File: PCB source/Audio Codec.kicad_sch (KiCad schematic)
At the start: 25 parts, among them J3 JST XH, U8 TDA7052A, U9 PCM2704CDBR, X1 X322512MSB4SI

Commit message: Figure out SSPND pin
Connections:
- net VDD_{int}: no longer U9.27 (~{SSPND})
- net VCCL: now reaches C35.1, U9.13 (VCCL)
- net VCCR: now reaches C38.1, U9.16 (VCCR)
- net VCCP: now reaches C39.1, U9.20 (VCCP)
- no-connect marks 5 -> 6
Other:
- moved on the sheet: C32, C33, C34, C35, C38, C39

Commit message: Prepare board for layout
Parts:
- removed R19: 1.5kΩ, PCM_JLCPCB:R_0402, symbol PCM_JLCPCB-Resistors:0402,1.5kΩ
- removed R20, R21: 22Ω, PCM_JLCPCB:R_0402, symbol PCM_JLCPCB-Resistors:0402,22Ω
- added R42: 1.5kΩ, PCM_JLCPCB:R_0603, symbol PCM_JLCPCB-Resistors:0603,1.5kΩ
- RV1: value 1Meg Bourns 3296 -> RM065 1Meg; footprint Potentiometer_THT:Potentiometer_Bourns_3296W_Vertical -> Potentiometer_THT:Potentiometer_Runtron_RM-065_Vertical
- U8: footprint (none) -> Package_SO:SO-8_3.9x4.9mm_P1.27mm
- U9: footprint PCM2704CDBR:SOP65P780X200-28N -> PCM2704:SOP65P780X200-28N
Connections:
- net VDD_{int}: now also R42.1
- net D+ renamed USB_AUDIO.D+
- net USB_AUDIO.D+: now also R42.2
- net D- renamed USB_AUDIO.D-

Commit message: Do buck Layout
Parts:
- removed R42: 1.5kΩ, PCM_JLCPCB:R_0603, symbol PCM_JLCPCB-Resistors:0603,1.5kΩ
- added R19: 1.5kΩ, PCM_JLCPCB:R_0402, symbol PCM_JLCPCB-Resistors:0402,1.5kΩ
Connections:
- net USB_AUDIO.D+: now also R19.2
- net VDD_{int}: now also R19.1
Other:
- moved on the sheet: C40

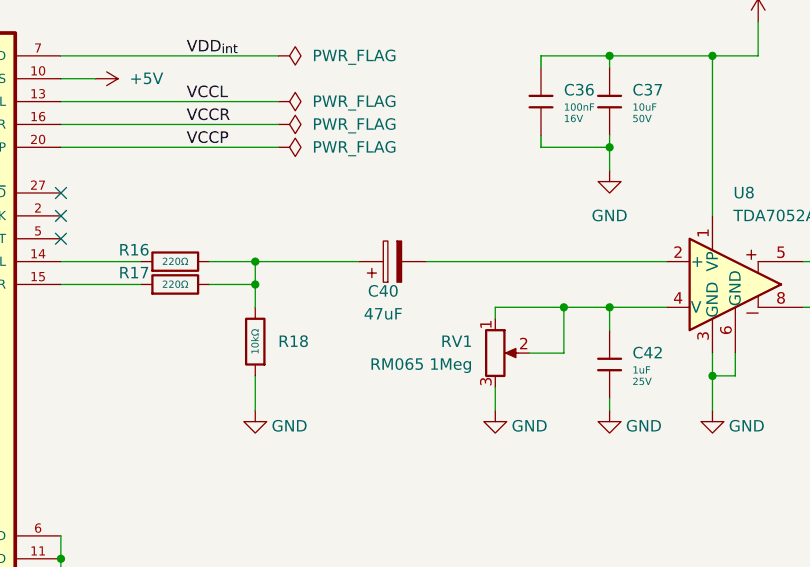
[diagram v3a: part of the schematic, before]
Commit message: Create v1 floorplan
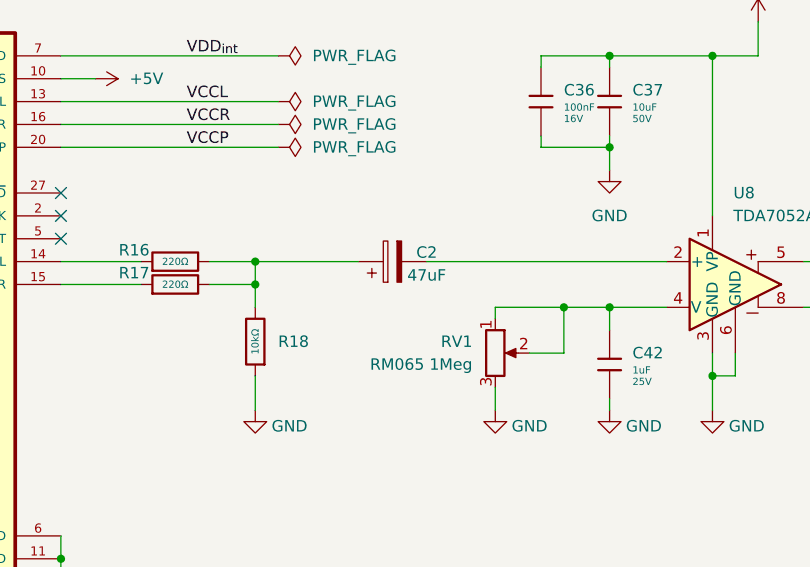
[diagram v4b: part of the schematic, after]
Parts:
- removed C40: 47uF, Capacitor_SMD:CP_Elec_6.3x5.4, symbol Device:C_Polarized
- added C2: 47uF, Capacitor_SMD:CP_Elec_4x5.4, symbol Device:C_Polarized
- C41: footprint Capacitor_SMD:CP_Elec_6.3x5.4 -> Capacitor_SMD:CP_Elec_4x5.4
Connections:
- net at R16.2, R17.2, R18.2: now also C2.1
- net at U8.2 (+): now also C2.2
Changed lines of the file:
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@@
 	)
 	(symbol
-		(lib_id "Device:C_Polarized")
-		(at 177.8 86.36 90)
-		(unit 1)
-		(exclude_from_sim no)
-		(in_bom yes)
-		(on_board yes)
-		(dnp no)
-		(property "Reference" "C40"
-			(at 176.784 89.662 90)
-			(effects
-				(font
-					(size 1.27 1.27)
-				)
-			)
-		)
-		(property "Value" "47uF"
-			(at 176.784 92.202 90)
-			(effects
-				(font
-					(size 1.27 1.27)
-				)
-			)
-		)
-		(property "Footprint" "Capacitor_SMD:CP_Elec_6.3x5.4"
-			(at 181.61 85.3948 0)
-			(effects
-				(font
-					(size 1.27 1.27)
-				)
-				(hide yes)
-			)
-		)
-		(property "Datasheet" "~"
-			(at 177.8 86.36 0)
-			(effects
-				(font
-					(size 1.27 1.27)
-				)
-				(hide yes)
-			)
-		)
-		(property "Description" "Polarized capacitor"
-			(at 177.8 86.36 0)
-			(effects
-				(font
-					(size 1.27 1.27)
-				)
-				(hide yes)
-			)
-		)
-		(property "LCSC" " C90276"
-			(at 177.8 86.36 90)
-			(effects
-				(font
-					(size 1.27 1.27)
-				)
-				(hide yes)
-			)
-		)
-		(property "MPN" "VT1V470M0605"
-			(at 177.8 86.36 90)
-			(effects
-				(font
-					(size 1.27 1.27)
-				)
-				(hide yes)
-			)
-		)
-		(pin "1"
-		)
-		(pin "2"
-		)
-		(instances
-			(project ""
-				(path "/3103c9de-f1ba-4d51-8bfc-798df1c75e2f/5c90feeb-24b4-4351-a3fd-4dbcb45d386c"
-					(reference "C40")
-					(unit 1)
-				)
-			)
-		)
-	)
-	(symbol
 		(lib_id "power:GND")
 		(at 96.52 160.02 0)
@@
 	)
 	(symbol
+		(lib_id "Device:C_Polarized")
+		(at 177.8 86.36 90)
+		(unit 1)
+		(exclude_from_sim no)
+		(in_bom yes)
+		(on_board yes)
+		(dnp no)
+		(property "Reference" "C2"
+			(at 181.61 85.344 90)
+			(effects
+				(font
+					(size 1.27 1.27)
+				)
+			)
+		)
+		(property "Value" "47uF"
+			(at 181.61 87.884 90)
+			(effects
+				(font
+					(size 1.27 1.27)
+				)
+			)
+		)
+		(property "Footprint" "Capacitor_SMD:CP_Elec_4x5.4"
+			(at 181.61 85.3948 0)
+			(effects
+				(font
+					(size 1.27 1.27)
+				)
+				(hide yes)
+			)
+		)
+		(property "Datasheet" "~"
+			(at 177.8 86.36 0)
+			(effects
+				(font
+					(size 1.27 1.27)
+				)
+				(hide yes)
+			)
+		)
+		(property "Description" "Polarized capacitor"
+			(at 177.8 86.36 0)
+			(effects
+				(font
+					(size 1.27 1.27)
+				)
+				(hide yes)
+			)
+		)
+		(property "LCSC" " C90276"
+			(at 177.8 86.36 90)
+			(effects
+				(font
+					(size 1.27 1.27)
+				)
+				(hide yes)
+			)
+		)
+		(property "MPN" "VT1V470M0605"
+			(at 177.8 86.36 90)
+			(effects
+				(font
+					(size 1.27 1.27)
+				)
+				(hide yes)
+			)
+		)
+		(pin "1"
+		)
+		(pin "2"
+		)
+		(instances
+			(project "OrangePie"
+				(path "/3103c9de-f1ba-4d51-8bfc-798df1c75e2f/5c90feeb-24b4-4351-a3fd-4dbcb45d386c"
+					(reference "C2")
+					(unit 1)
+				)
+			)
+		)
+	)
+	(symbol
 		(lib_id "PCM_JLCPCB-Capacitors:0402,1uF")
 		(at 190.5 139.7 90)
@@
 			)
 		)
-		(property "Footprint" "Capacitor_SMD:CP_Elec_6.3x5.4"
+		(property "Footprint" "Capacitor_SMD:CP_Elec_4x5.4"
 			(at 81.28 97.4852 0)
 			(effects

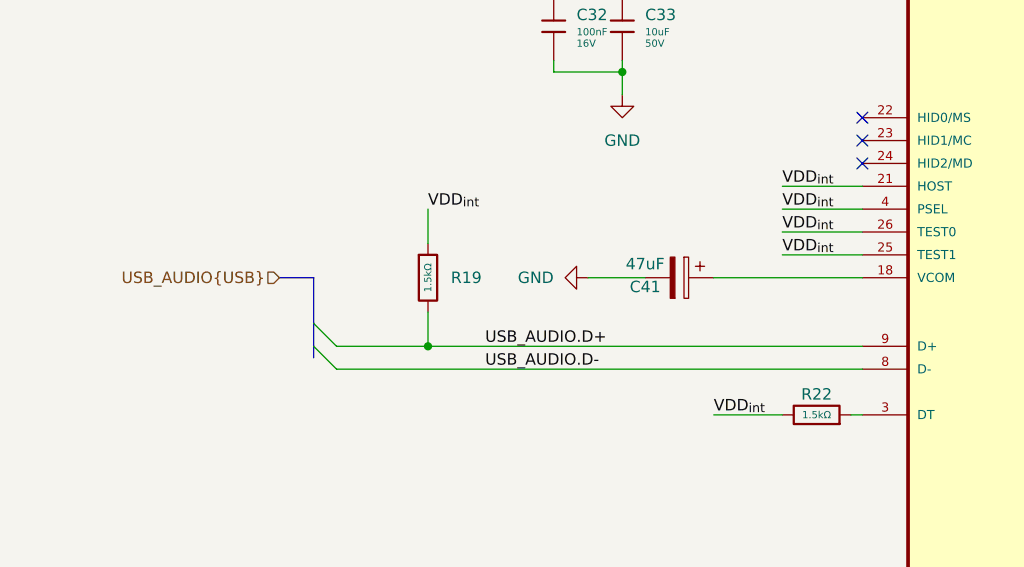
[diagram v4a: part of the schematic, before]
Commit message: Add 22R resistors to USB
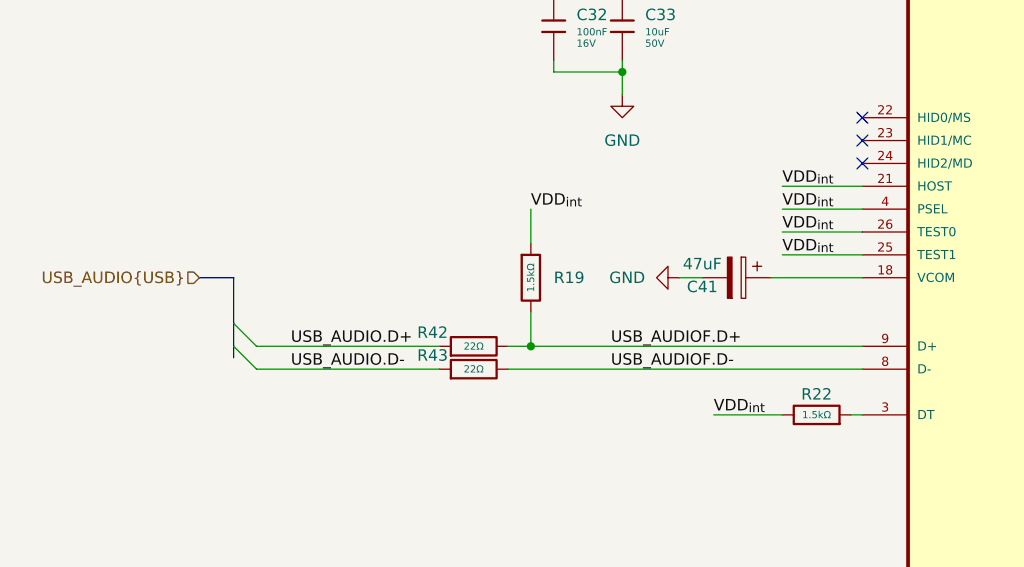
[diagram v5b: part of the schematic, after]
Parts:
- added R42, R43: 22Ω, PCM_JLCPCB:R_0402, symbol PCM_JLCPCB-Resistors:0402,22Ω
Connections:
- net USB_AUDIO.D+: now also R42.1; no longer R19.2, U9.9 (D+)
- net USB_AUDIO.D-: now also R43.1; no longer U9.8 (D-)
- new net USB_AUDIOF.D+: R19.2, R42.2, U9.9 (D+)
- new net USB_AUDIOF.D-: R43.2, U9.8 (D-)
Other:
- moved on the sheet: C41, R19

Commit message: Fix schematic
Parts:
- removed C2, C41: 47uF, Capacitor_SMD:CP_Elec_4x5.4, symbol Device:C_Polarized
- removed C43, C44: 22pF, PCM_JLCPCB:C_0402, symbol PCM_JLCPCB-Capacitors:0402,22pF
- added C2, C41, C48: 47uF 50V RVT1H470M0607, Capacitor_SMD:CP_Elec_6.3x7.7, symbol Device:C_Polarized_Small
- added C43, C44: 33pF, PCM_JLCPCB:C_0402, symbol PCM_JLCPCB-Capacitors:0402,33pF
- added Q10, Q6: AO3401A, PCM_JLCPCB:Q_SOT-23, symbol PCM_JLCPCB-Transistors:PMOS,AO3401A
- added Q7: AO3400A, PCM_JLCPCB:Q_SOT-23, symbol PCM_JLCPCB-Transistors:NMOS,AO3400A
- added R46, R55, R58: 10kΩ, PCM_JLCPCB:R_0402, symbol PCM_JLCPCB-Resistors:0402,10kΩ
- added R59, R60, R61: 22Ω, PCM_JLCPCB:R_0402, symbol PCM_JLCPCB-Resistors:0402,22Ω
- C32, C36: Stock 27771805 -> 19831671
- C33, C37: Price 0.067USD -> 0.069USD; Stock 1423931 -> 1211974
- C34, C35, C38, C39, C42: Stock 8324208 -> 6453835
- R16, R17: Stock 734290 -> 927669
- R18: Stock 6666349 -> 13746052
- R19, R22: Stock 778464 -> 1074828
- R42, R43: Stock 2497993 -> 2158519
- U9: footprint PCM2704:SOP65P780X200-28N -> PCM2704CDBR:SOP65P780X200-28N
- X1: Frequency Stability ±30ppm -> ±20ppm; Normal Temperature Frequency Tolerance (none) -> ±10ppm; Price 0.074USD -> 0.069USD; Stock 388238 -> 141095; Type (none) -> Surface Mount Crystal
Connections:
- net +5V: now also C48.1, Q7.3 (D), R46.1, R55.2; no longer U9.10 (VBUS)
- net GND: now also C41.2, C43.2, C44.2, C48.2, Q10.2 (S), Q6.2 (S), R58.1
- net at R16.2, R17.2, R18.2: now also C2.1
- net at U9.1 (XTO), X1.3 (OSC): now also C44.1
- net at U9.18 (VCOM): now also C41.1
- net at U9.28 (XTI), X1.1 (OSC): now also C43.1
- net at U8.2 (+): now also C2.2
- new net: Q10.1 (G), R58.2, R61.2
- new net: Q7.1 (G), R46.2, R59.1
- new net: Q6.3 (D), R59.2
- new net: Q10.3 (D), R55.1, R60.1
- new net: Q6.1 (G), R60.2
- new net DAC reset: R61.1
- new net VBUS: Q7.2 (S), U9.10 (VBUS)
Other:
- note added: "RESET"
- note added: "c stray approx 4pf C1 = C2 = 2*(CL-Cs) = 32 closest value 33"
- moved on the sheet: C32, C33, C34, C35, C36, C37, C38, C39, C42, J3, R16, R17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

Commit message: [3] Start layout
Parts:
- removed C2: 47uF 50V RVT1H470M0607, Capacitor_SMD:CP_Elec_6.3x7.7, symbol Device:C_Polarized_Small
- added C40: 10uF, PCM_JLCPCB:C_0805, symbol PCM_JLCPCB-Capacitors:0805,10uF,(2)
- U9: footprint PCM2704CDBR:SOP65P780X200-28N -> Package_SO:SSOP-28_5.3x10.2mm_P0.65mm
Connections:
- net at R16.2, R17.2, R18.2: now also C40.2
- net at U8.2 (+): now also C40.1
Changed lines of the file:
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@@
 	)
 	(junction
-		(at 190.5 63.5)
-		(diameter 0)
-		(color 0 0 0 0)
-	)
-	(junction
 		(at 99.06 50.8)
 		(diameter 0)
@@
 	)
 	(junction
+		(at 190.5 63.5)
+		(diameter 0)
+		(color 0 0 0 0)
+	)
+	(junction
 		(at 227.33 109.22)
 		(diameter 0)
@@
 	(wire
 		(pts
+			(xy 190.5 63.5) (xy 201.93 63.5)
+		)
+		(stroke
+			(width 0)
+			(type default)
+		)
+	)
+	(wire
+		(pts
 			(xy 168.91 101.6) (xy 168.91 104.14)
 		)
@@
 	(wire
 		(pts
-			(xy 190.5 63.5) (xy 203.2 63.5)
-		)
-		(stroke
-			(width 0)
-			(type default)
-		)
-	)
-	(wire
-		(pts
 			(xy 124.46 71.12) (xy 133.35 71.12)
 		)
@@
 	(wire
 		(pts
+			(xy 209.55 63.5) (xy 236.22 63.5)
+		)
+		(stroke
+			(width 0)
+			(type default)
+		)
+	)
+	(wire
+		(pts
 			(xy 54.61 158.75) (xy 54.61 161.29)
 		)
@@
 	(wire
 		(pts
-			(xy 171.45 43.18) (xy 168.91 43.18)
-		)
-		(stroke
-			(width 0)
-			(type default)
-		)
-	)
-	(wire
-		(pts
 			(xy 261.62 67.31) (xy 260.35 67.31)
 		)
@@
 	(wire
 		(pts
-			(xy 208.28 63.5) (xy 236.22 63.5)
-		)
-		(stroke
-			(width 0)
-			(type default)
-		)
-	)
-	(wire
-		(pts
 			(xy 179.07 135.89) (xy 179.07 137.16)
 		)
@@
 		)
 	)
-	(label "VCCR"
-		(at 182.88 48.26 0)
+	(label "VBUS"
+		(at 168.91 43.18 0)
 		(effects
 			(font
@@
 		)
 	)
-	(label "VCCP"
-		(at 207.01 116.84 0)
+	(label "VCCR"
+		(at 182.88 48.26 0)
 		(effects
 			(font
@@
 		)
 	)
-	(label "VDD_{int}"
-		(at 96.52 66.04 0)
+	(label "VCCP"
+		(at 207.01 116.84 0)
 		(effects
 			(font
@@
 		)
 	)
-	(label "VBUS"
-		(at 171.45 43.18 0)
+	(label "VDD_{int}"
+		(at 96.52 66.04 0)
 		(effects
 			(font
@@
 			)
 		)
-		(property "Footprint" "PCM2704CDBR:SOP65P780X200-28N"
+		(property "Footprint" "Package_SO:SSOP-28_5.3x10.2mm_P0.65mm"
 			(at 151.13 73.66 0)
 			(effects
@@
 	)
 	(symbol
-		(lib_id "Device:C_Polarized_Small")
-		(at 205.74 63.5 90)
-		(unit 1)
-		(exclude_from_sim no)
-		(in_bom yes)
-		(on_board yes)
-		(dnp no)
-		(fields_autoplaced yes)
-		(property "Reference" "C2"
-			(at 205.1939 57.15 90)
-			(effects
-				(font
-					(size 1.27 1.27)
-				)
-			)
-		)
-		(property "Value" "47uF 50V RVT1H470M0607"
-			(at 205.1939 59.69 90)
-			(effects
-				(font
-					(size 1.27 1.27)
-				)
-			)
-		)
-		(property "Footprint" "Capacitor_SMD:CP_Elec_6.3x7.7"
-			(at 205.74 63.5 0)
-			(effects
-				(font
-					(size 1.27 1.27)
-				)
-				(hide yes)
-			)
-		)
-		(property "Datasheet" "~"
-			(at 205.74 63.5 0)
-			(effects
-				(font
-					(size 1.27 1.27)
-				)
-				(hide yes)
-			)
-		)
-		(property "Description" "Polarized capacitor, small symbol"
-			(at 205.74 63.5 0)
-			(effects
-				(font
-					(size 1.27 1.27)
-				)
-				(hide yes)
-			)
-		)
-		(pin "1"
-		)
-		(pin "2"
-		)
-		(instances
-			(project "OrangePie"
-				(path "/3103c9de-f1ba-4d51-8bfc-798df1c75e2f/5c90feeb-24b4-4351-a3fd-4dbcb45d386c"
-					(reference "C2")
-					(unit 1)
-				)
-			)
-		)
-	)
-	(symbol
 		(lib_id "Connector_Generic:Conn_01x02")
 		(at 266.7 64.77 0)
@@
 					(unit 1)
 				)
+			)
+		)
+	)
+	(symbol
+		(lib_id "PCM_JLCPCB-Capacitors:0805,10uF,(2)")
+		(at 205.74 63.5 270)
+		(unit 1)
+		(exclude_from_sim no)
+		(in_bom yes)
+		(on_board yes)
+		(dnp no)
+		(fields_autoplaced yes)
+		(property "Reference" "C40"
+			(at 205.74 54.61 90)
+			(effects
+				(font
+					(size 1.27 1.27)
+				)
+			)
+		)
+		(property "Value" "10uF"
+			(at 205.74 57.15 90)
+			(effects
+				(font
+					(size 0.8 0.8)
+				)
+			)
+		)
+		(property "Footprint" "PCM_JLCPCB:C_0805"
+			(at 205.74 61.722 90)
+			(effects
+				(font
+					(size 1.27 1.27)
+				)
+				(hide yes)
+			)
+		)
+		(property "Datasheet" "https://www.lcsc.com/datasheet/lcsc_datasheet_2411041759_Murata-Electronics-GRM21BR61H106KE43L_C440198.pdf"
+			(at 205.74 63.5 0)
+			(effects
+				(font
+					(size 1.27 1.27)
+				)
+				(hide yes)
+			)
+		)
+		(property "Description" "50V 10uF X5R ±10% 0805 Multilayer Ceramic Capacitors MLCC - SMD/SMT ROHS"
+			(at 205.74 63.5 0)
+			(effects
+				(font
+					(size 1.27 1.27)
+				)
+				(hide yes)
+			)
+		)
+		(property "LCSC" "C440198"
+			(at 205.74 63.5 0)
+			(effects
+				(font
+					(size 1.27 1.27)
+				)
+				(hide yes)
+			)
+		)
+		(property "Stock" "1211974"
+			(at 205.74 63.5 0)
+			(effects
+				(font
+					(size 1.27 1.27)
+				)
+				(hide yes)
+			)
+		)
+		(property "Price" "0.069USD"
+			(at 205.74 63.5 0)
+			(effects
+				(font
+					(size 1.27 1.27)
+				)
+				(hide yes)
+			)
+		)
+		(property "Process" "SMT"
+			(at 205.74 63.5 0)
+			(effects
+				(font
+					(size 1.27 1.27)
+				)
+				(hide yes)
+			)
+		)
+		(property "Minimum Qty" "5"
+			(at 205.74 63.5 0)
+			(effects
+				(font
+					(size 1.27 1.27)
+				)
+				(hide yes)
+			)
+		)
+		(property "Attrition Qty" "4"
+			(at 205.74 63.5 0)
+			(effects
+				(font
+					(size 1.27 1.27)
+				)
+				(hide yes)
+			)
+		)
+		(property "Class" "Basic Component"
+			(at 205.74 63.5 0)
+			(effects
+				(font
+					(size 1.27 1.27)
+				)
+				(hide yes)
+			)
+		)
+		(property "Category" "Capacitors,Multilayer Ceramic Capacitors MLCC - SMD/SMT"
+			(at 205.74 63.5 0)
+			(effects
+				(font
+					(size 1.27 1.27)
+				)
+				(hide yes)
+			)
+		)
+		(property "Manufacturer" "Murata Electronics"
+			(at 205.74 63.5 0)
+			(effects
+				(font
+					(size 1.27 1.27)
+				)
+				(hide yes)
+			)
+		)
+		(property "Part" "GRM21BR61H106KE43L"
+			(at 205.74 63.5 0)
+			(effects
+				(font
+					(size 1.27 1.27)
+				)
+				(hide yes)
+			)
+		)
+		(property "Voltage Rated" "50V"
+			(at 205.74 59.69 90)
+			(effects
+				(font
+					(size 0.8 0.8)
+				)
+			)
+		)
+		(property "Tolerance" "±10%"
+			(at 205.74 63.5 0)
+			(effects
+				(font
+					(size 1.27 1.27)
+				)
+				(hide yes)
+			)
+		)
+		(property "Capacitance" "10uF"
+			(at 205.74 63.5 0)
+			(effects
+				(font
+					(size 1.27 1.27)
+				)
+				(hide yes)
+			)
+		)
+		(property "Temperature Coefficient" "X5R"
+			(at 205.74 63.5 0)
+			(effects
+				(font
+					(size 1.27 1.27)
+				)
+				(hide yes)
+			)
+		)
+		(pin "1"
+		)
+		(pin "2"
+		)
+		(instances
+			(project "OrangePie"
+				(path "/3103c9de-f1ba-4d51-8bfc-798df1c75e2f/5c90feeb-24b4-4351-a3fd-4dbcb45d386c"
+					(reference "C40")
+					(unit 1)
+				)

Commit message: [3] Finish pcb
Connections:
- net +5V: no longer C32.1, C33.2
- net VBUS: now also C32.1, C33.2
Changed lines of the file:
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@@
-	)
-	(junction
-		(at 106.68 40.64)
-		(diameter 0)
-		(color 0 0 0 0)
 	)
 	(junction
@@
 	)
 	(junction
-		(at 99.06 40.64)
-		(diameter 0)
-		(color 0 0 0 0)
-	)
-	(junction
 		(at 241.3 40.64)
 		(diameter 0)
@@
 	(wire
 		(pts
-			(xy 92.71 40.64) (xy 99.06 40.64)
-		)
-		(stroke
-			(width 0)
-			(type default)
-		)
-	)
-	(wire
-		(pts
 			(xy 222.25 113.03) (xy 227.33 113.03)
 		)
@@
 	(wire
 		(pts
-			(xy 92.71 43.18) (xy 92.71 40.64)
-		)
-		(stroke
-			(width 0)
-			(type default)
-		)
-	)
-	(wire
-		(pts
 			(xy 222.25 49.53) (xy 222.25 50.8)
 		)
@@
 	(wire
 		(pts
-			(xy 106.68 38.1) (xy 106.68 40.64)
+			(xy 92.71 38.1) (xy 92.71 43.18)
 		)
 		(stroke
@@
 	(label "VCCP"
 		(at 207.01 116.84 0)
+		(effects
+			(font
+				(size 1.27 1.27)
+			)
+			(justify left bottom)
+		)
+	)
+	(label "VBUS"
+		(at 106.68 40.64 0)
 		(effects
 			(font
@@
 	(symbol
 		(lib_id "power:+5V")
-		(at 106.68 38.1 0)
+		(at 92.71 38.1 0)
 		(unit 1)
 		(exclude_from_sim no)
@@
 		(fields_autoplaced yes)
 		(property "Reference" "#PWR074"
-			(at 106.68 41.91 0)
+			(at 92.71 41.91 0)
 			(effects
 				(font
@@
 		)
 		(property "Value" "+5V"
-			(at 106.68 33.02 0)
+			(at 92.71 33.02 0)
 			(effects
 				(font
@@
 		)
 		(property "Footprint" ""
-			(at 106.68 38.1 0)
+			(at 92.71 38.1 0)
 			(effects
 				(font
@@
 		)
 		(property "Datasheet" ""
-			(at 106.68 38.1 0)
+			(at 92.71 38.1 0)
 			(effects
 				(font
@@
 		)
 		(property "Description" "Power symbol creates a global label with name \"+5V\""
-			(at 106.68 38.1 0)
-			(effects
-				(font
+			(at 92.71 38.1 0)
+			(effects
+				(font
